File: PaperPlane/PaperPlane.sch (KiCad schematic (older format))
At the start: 6 parts

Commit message: PCB sch
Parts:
- renumbered Cin to Cin1, Cout to Cout1, L to L1, Rfbb to Rfbb1, Rfbt to Rfbt1, TLV62568DBVR to TLV62568DBVR1
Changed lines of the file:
@@
 $EndDescr
 $Comp
-L Device:C Cin
+L Device:C Cin1
 U 1 1 5F9CD19E
 P 5000 2600
-F 0 "Cin" H 5115 2646 50  0000 L CNN
+F 0 "Cin1" H 5115 2646 50  0000 L CNN
 F 1 "4.7uF" H 5115 2555 50  0000 L CNN
 F 2 "Capacitor_SMD:C_0603_1608Metric" H 5038 2450 50  0001 C CNN
@@
 $EndComp
 $Comp
-L Device:L L
+L Device:L L1
 U 1 1 5F9CE3A9
 P 6150 2150
-F 0 "L" V 6340 2150 50  0000 C CNN
+F 0 "L1" V 6340 2150 50  0000 C CNN
 F 1 "2.2uH 2.6A" V 6249 2150 50  0000 C CNN
 F 2 "Inductor_SMD:L_Taiyo-Yuden_NR-50xx_HandSoldering" H 6150 2150 50  0001 C CNN
@@
 $EndComp
 $Comp
-L Device:R Rfbt
+L Device:R Rfbt1
 U 1 1 5F9CEE79
 P 6400 2400
-F 0 "Rfbt" H 6470 2446 50  0000 L CNN
+F 0 "Rfbt1" H 6470 2446 50  0000 L CNN
 F 1 "453k" H 6470 2355 50  0000 L CNN
 F 2 "Resistor_SMD:R_0603_1608Metric" V 6330 2400 50  0001 C CNN
@@
 $EndComp
 $Comp
-L Device:R Rfbb
+L Device:R Rfbb1
 U 1 1 5F9CF952
 P 6400 2900
-F 0 "Rfbb" H 6470 2946 50  0000 L CNN
+F 0 "Rfbb1" H 6470 2946 50  0000 L CNN
 F 1 "100k" H 6470 2855 50  0000 L CNN
 F 2 "Resistor_SMD:R_0603_1608Metric" V 6330 2900 50  0001 C CNN
@@
 $EndComp
 $Comp
-L Device:C Cout
+L Device:C Cout1
 U 1 1 5F9D00FB
 P 6850 2600
-F 0 "Cout" H 6965 2646 50  0000 L CNN
+F 0 "Cout1" H 6965 2646 50  0000 L CNN
 F 1 "10uF" H 6965 2555 50  0000 L CNN
 F 2 "Capacitor_SMD:C_0603_1608Metric" H 6888 2450 50  0001 C CNN
@@
 Connection ~ 6850 2150
 $Comp
-L Regulator_Switching:TLV62568DBV TLV62568DBVR
+L Regulator_Switching:TLV62568DBV TLV62568DBVR1
 U 1 1 5F9D1940
 P 5550 2250
-F 0 "TLV62568DBVR" H 5550 2617 50  0000 C CNN
+F 0 "TLV62568DBVR1" H 5550 2617 50  0000 C CNN
 F 1 "TLV62568DBV" H 5550 2526 50  0000 C CNN
 F 2 "Package_TO_SOT_SMD:SOT-23-5" H 5600 2000 50  0001 L CIN

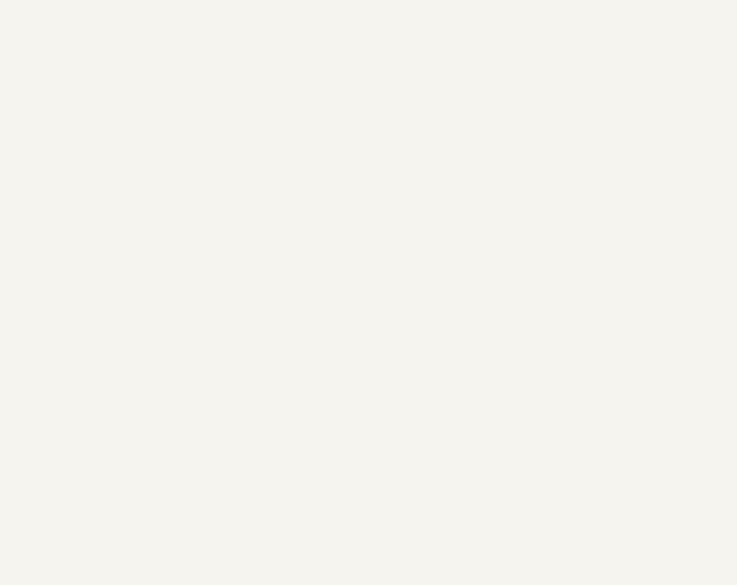
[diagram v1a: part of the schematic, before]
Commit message: Add STM32G031K8T6
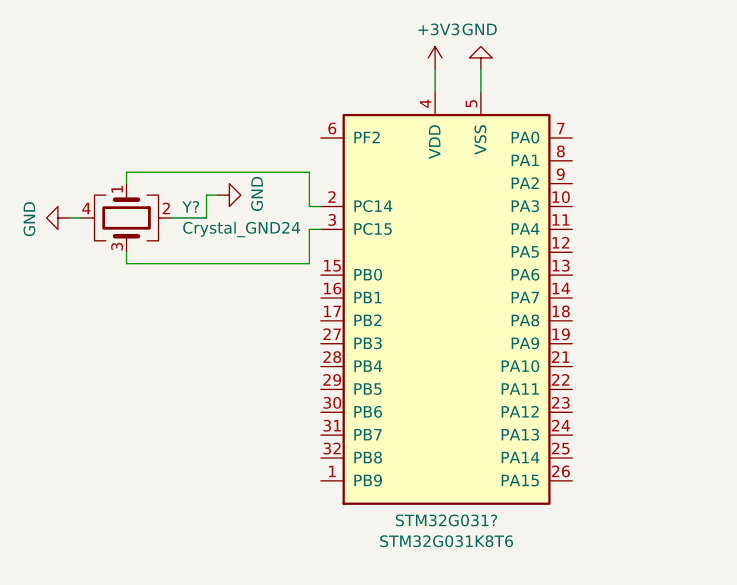
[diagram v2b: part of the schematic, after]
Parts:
- added STM32G031?: STM32G031K8T6, Package_QFP:LQFP-32_7x7mm_P0.8mm, symbol PaperPlane:STM32G031K8T6
- added Y?: Crystal_GND24, Crystal:Crystal_SMD_3225-4Pin_3.2x2.5mm, symbol Device:Crystal_GND24
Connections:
- net +3V3: now also STM32G031?.4 (VDD)
- net GND: now also STM32G031?.5 (VSS), Y?.2, Y?.4
- new net: STM32G031?.2 (PC14), Y?.1
- new net: STM32G031?.3 (PC15), Y?.3
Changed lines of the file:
@@
 	1    0    0    -1
 $EndComp
+$Comp
+L PaperPlane:STM32G031K8T6 STM32G031?
+U 1 1 5F9E49FA
+P 2750 2350
+F 0 "STM32G031?" H 2700 1375 50  0000 C CNN
+F 1 "STM32G031K8T6" H 2700 1284 50  0000 C CNN
+F 2 "Package_QFP:LQFP-32_7x7mm_P0.8mm" H 2750 1150 50  0001 C CNN
+F 3 "" H 2750 2350 50  0001 C CNN
+	1    2750 2350
+	1    0    0    -1
+$EndComp
+$Comp
+L power:+3V3 #PWR?
+U 1 1 5F9EB810
+P 2650 1350
+F 0 "#PWR?" H 2650 1200 50  0001 C CNN
+F 1 "+3V3" H 2665 1523 50  0000 C CNN
+F 2 "" H 2650 1350 50  0001 C CNN
+F 3 "" H 2650 1350 50  0001 C CNN
+	1    2650 1350
+	1    0    0    -1
+$EndComp
+$Comp
+L power:GND #PWR?
+U 1 1 5F9EC827
+P 2850 1350
+F 0 "#PWR?" H 2850 1100 50  0001 C CNN
+F 1 "GND" H 2855 1177 50  0000 C CNN
+F 2 "" H 2850 1350 50  0001 C CNN
+F 3 "" H 2850 1350 50  0001 C CNN
+	1    2850 1350
+	-1   0    0    1
+$EndComp
+Wire Wire Line
+	2650 1350 2650 1450
+Wire Wire Line
+	2850 1350 2850 1450
+Wire Wire Line
+	2100 1950 2150 1950
+Wire Wire Line
+	2150 2050 2100 2050
+Wire Wire Line
+	2100 2050 2100 2200
+Wire Wire Line
+	2100 2200 1300 2200
+Wire Wire Line
+	1300 2200 1300 2150
+Wire Wire Line
+	1300 1850 1300 1800
+Wire Wire Line
+	2100 1800 2100 1950
+Wire Wire Line
+	1300 1800 2100 1800
+$Comp
+L Device:Crystal_GND24 Y?
+U 1 1 5F9EE8E5
+P 1300 2000
+F 0 "Y?" V 1254 2244 50  0000 L CNN
+F 1 "Crystal_GND24" V 1345 2244 50  0000 L CNN
+F 2 "Crystal:Crystal_SMD_3225-4Pin_3.2x2.5mm" H 1300 2000 50  0001 C CNN
+F 3 "~" H 1300 2000 50  0001 C CNN
+	1    1300 2000
+	0    1    1    0
+$EndComp
+$Comp
+L power:GND #PWR?
+U 1 1 5F9F59AA
+P 1700 1900
+F 0 "#PWR?" H 1700 1650 50  0001 C CNN
+F 1 "GND" H 1705 1727 50  0000 C CNN
+F 2 "" H 1700 1900 50  0001 C CNN
+F 3 "" H 1700 1900 50  0001 C CNN
+	1    1700 1900
+	0    -1   -1   0
+$EndComp
+Wire Wire Line
+	1500 2000 1650 2000
+Wire Wire Line
+	1650 2000 1650 1900
+Wire Wire Line
+	1650 1900 1700 1900
+$Comp
+L power:GND #PWR?
+U 1 1 5F9F92D6
+P 1050 2000
+F 0 "#PWR?" H 1050 1750 50  0001 C CNN
+F 1 "GND" H 1055 1827 50  0000 C CNN
+F 2 "" H 1050 2000 50  0001 C CNN
+F 3 "" H 1050 2000 50  0001 C CNN
+	1    1050 2000
+	0    1    1    0
+$EndComp
+Wire Wire Line
+	1050 2000 1100 2000
 $EndSCHEMATC

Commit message: HalfFinish
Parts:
- added BATT1, MOTOR1: Conn_01x02_Male, Connector_JST:JST_PH_B2B-PH-K_1x02_P2.00mm_Vertical, symbol Connector:Conn_01x02_Male
- added CMotor1, CMotor2, CRST1: 0.1uF, Capacitor_SMD:C_0603_1608Metric, symbol Device:C
- added LED1, ON1: LED, LED_SMD:LED_0603_1608Metric, symbol Device:LED
- added R-RST1, RBOOT1: 10k, Resistor_SMD:R_0603_1608Metric, symbol Device:R
- added RLED1, RON1: 1k, Resistor_SMD:R_0603_1608Metric, symbol Device:R
- added RRX1, RTX1: 22R, Resistor_SMD:R_0603_1608Metric, symbol Device:R
- added SW-RST1: SW_Push, Switches:TACTILE_SWITCH_SMD_6.0X3.5MM, symbol Switch:SW_Push
- added Servo1, Servo2: Conn_01x03_Male, Connector_Hirose:Hirose_DF13-03P-1.25DSA_1x03_P1.25mm_Vertical, symbol Connector:Conn_01x03_Male
- added Servo3, Servo4: Conn_01x03_Male, Connector_PinHeader_2.54mm:PinHeader_1x03_P2.54mm_Horizontal, symbol Connector:Conn_01x03_Male
- added U1: MPU-6050, Sensor_Motion:InvenSense_QFN-24_4x4mm_P0.5mm, symbol Sensor_Motion:MPU-6050
- added U2: ESP32-WROOM-32, RF_Module:ESP32-WROOM-32, symbol RF_Module:ESP32-WROOM-32
- added U3: DRV8837C, Package_SON:WSON-8-1EP_2x2mm_P0.5mm_EP0.9x1.6mm, symbol Driver_Motor:DRV8837C
- added UART1: Conn_01x04_Female, Connector_PinSocket_2.54mm:PinSocket_1x04_P2.54mm_Vertical, symbol Connector:Conn_01x04_Female
- gave numbers to parts that had none: 2
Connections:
- net +3V3: now also CMotor1.2, ON1.2 (A), R-RST1.1, U3.8 (VCC), UART1.1 (Pin_1)
- net +3V8: now also BATT1.2 (Pin_2), CMotor2.1, Servo1.2 (Pin_2), Servo2.2 (Pin_2), Servo3.2 (Pin_2), Servo4.2 (Pin_2), U3.1 (VM)
- net GND: now also BATT1.1 (Pin_1), CMotor1.1, CMotor2.2, CRST1.2, RBOOT1.2, RLED1.2, RON1.2, SW-RST1.2, Servo1.3 (Pin_3), Servo2.3 (Pin_3), Servo3.3 (Pin_3), Servo4.3 (Pin_3), U3.4 (GND), U3.9 (GND), UART1.2 (Pin_2)
- net LED: now reaches STM32G311.1 (PB9)
- net LED: now also LED1.2 (A)
- net USART1-TX: now reaches STM32G311.19 (PA9)
- net USART1-TX: now also RRX1.2
- net USART1-RX: now reaches STM32G311.21 (PA10)
- net USART1-RX: now also RTX1.2
- net PA14-BOOT0: now reaches STM32G311.25 (PA14)
- net PA14-BOOT0: now also RBOOT1.1
- net USART2-RX: now reaches STM32G311.26 (PA15)
- net NRST: now reaches STM32G311.6 (PF2)
- net NRST: now also CRST1.1, R-RST1.2, SW-RST1.1
- new net: ON1.1 (K), RON1.1
- new net: LED1.1 (K), RLED1.1
- new net: RRX1.1, UART1.3 (Pin_3)
- new net: RTX1.1, UART1.4 (Pin_4)
- new net: MOTOR1.2 (Pin_2), U3.2 (OUT1)
- new net: MOTOR1.1 (Pin_1), U3.3 (OUT2)
- new net: U2.1 (GND), U2.15 (GND), U2.38 (GND), U2.39 (GND)
- new net Servo1: Servo1.1 (Pin_1), Servo3.1 (Pin_1)
- new net Servo2: Servo2.1 (Pin_1), Servo4.1 (Pin_1)
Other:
- moved on the sheet: Cin1, Cout1, L1, Rfbb1, Rfbt1, TLV62568DBVR1

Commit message: ADD swdio swclk
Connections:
- net SWDIO: now reaches STM32G311.24 (PA13)
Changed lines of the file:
@@
 Wire Wire Line
 	3250 3150 3400 3150
-Wire Wire Line
-	3250 3050 3950 3050
 Text Label 3400 3150 0    50   ~ 0
 USART2-RX
@@
 	1    0    0    -1
 $EndComp
+Wire Wire Line
+	3250 2950 3400 2950
+Text Label 3400 2950 0    50   ~ 0
+SWDIO
+Text Label 4500 3050 0    50   ~ 0
+SWCLK
+Wire Wire Line
+	3250 3050 4500 3050
 $EndSCHEMATC
